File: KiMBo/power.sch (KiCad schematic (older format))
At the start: 30 parts

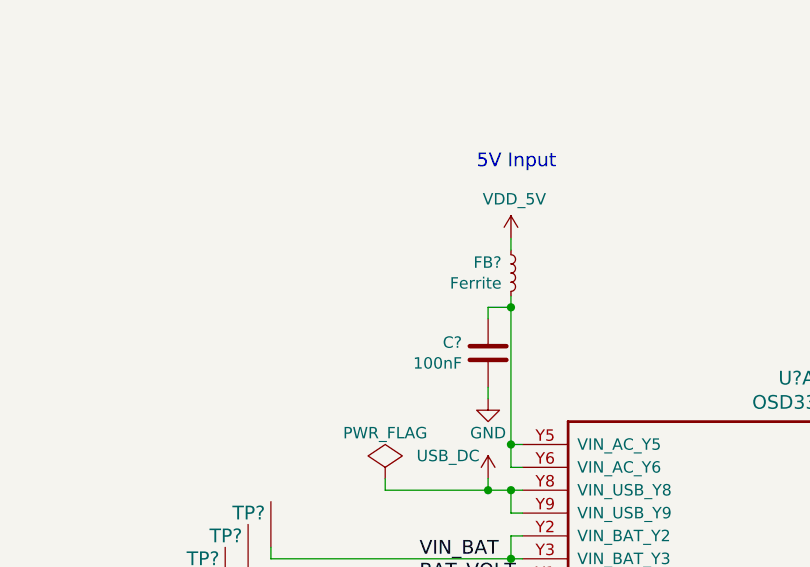
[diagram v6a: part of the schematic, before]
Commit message: Update ferrite values, select fuse based on interrupt rating
The PSU needs to be able to supply at LEAST 25A to blow the fuse
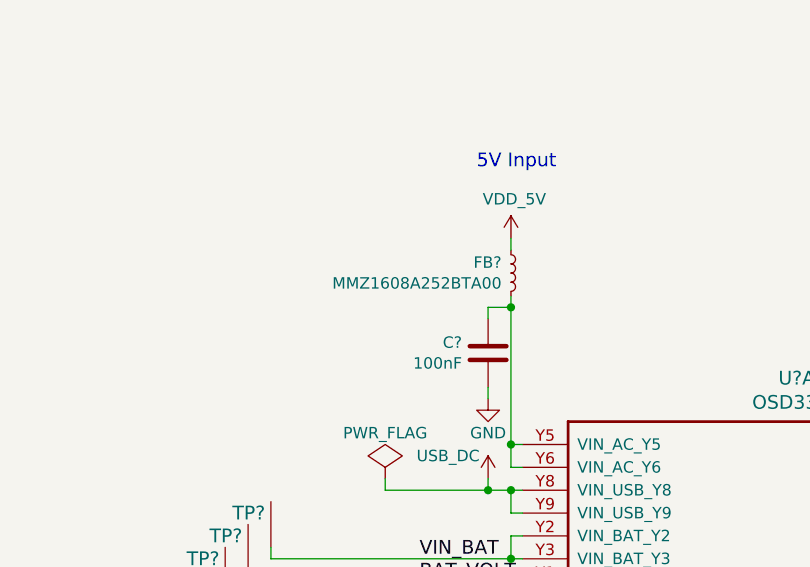
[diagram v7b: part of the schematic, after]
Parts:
- FB?: value Ferrite -> MMZ1608A252BTA00
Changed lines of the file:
@@
 P 6900 4000
 F 0 "FB?" H 6859 3954 50  0000 R CNN
-F 1 "Ferrite" H 6859 4045 50  0000 R CNN
+F 1 "MMZ1608A252BTA00" H 6859 4045 50  0000 R CNN
 F 2 "" H 6900 4000 50  0000 C CNN
 F 3 "" H 6900 4000 50  0000 C CNN
